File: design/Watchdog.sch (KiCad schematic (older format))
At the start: 23 parts, among them U401 74LV14, U402 74LVC2G00, U403 STWD100xxWY, U404 STWD100xxWY, U405 74AHC157

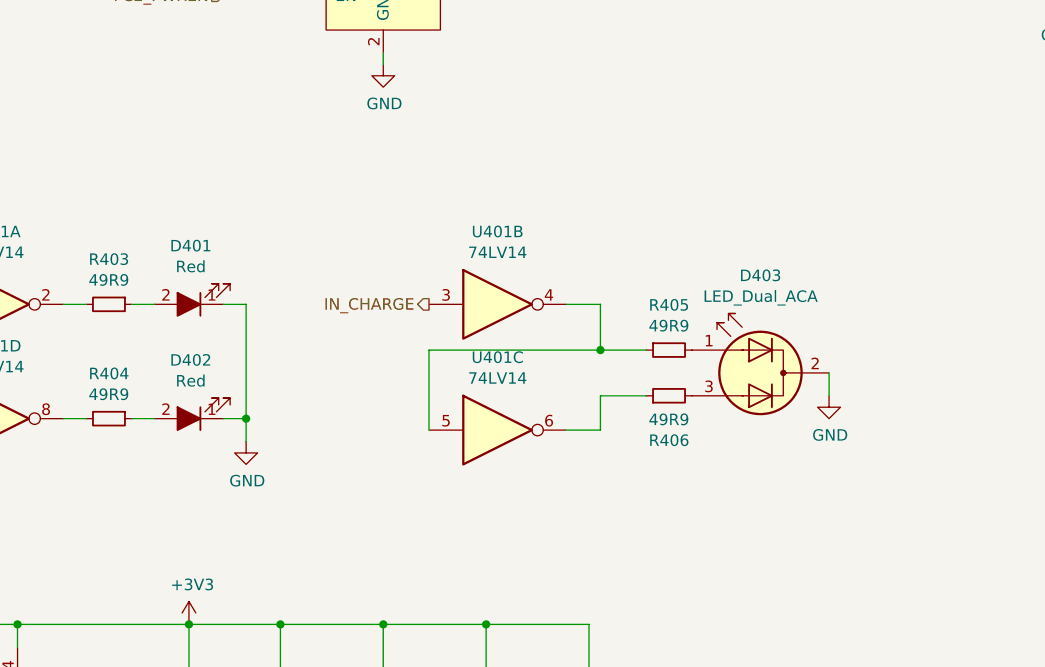
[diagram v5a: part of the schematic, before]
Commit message: Adding smaller light pipe and compressing power input
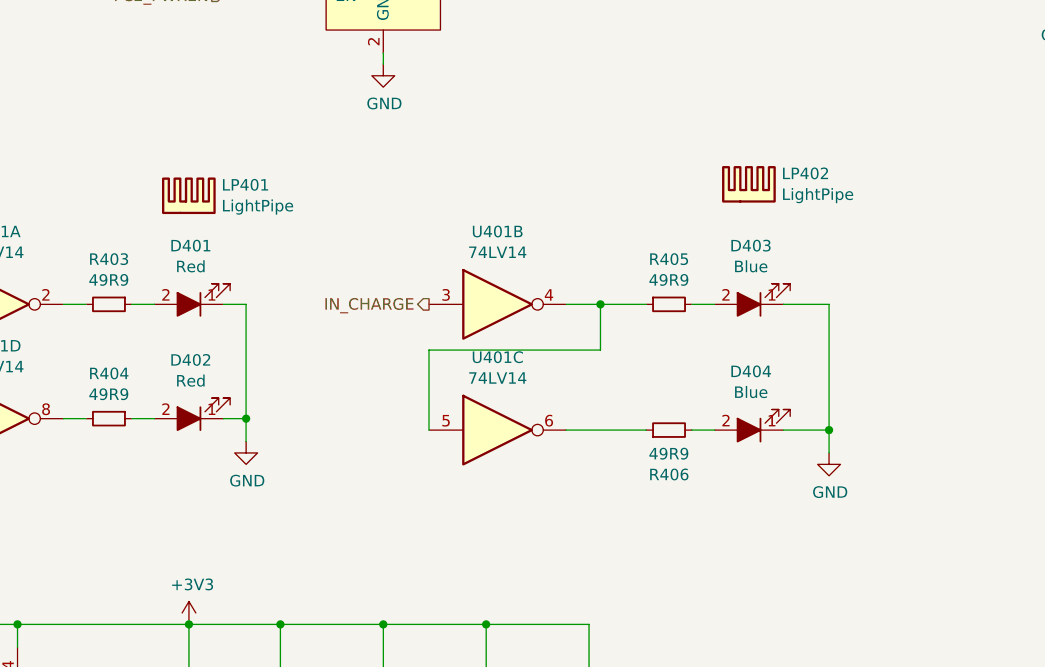
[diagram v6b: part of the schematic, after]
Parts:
- removed D403: LED_Dual_ACA, LEDs:WP130WDT, symbol Device:LED_Dual_ACA
- added D403, D404: Blue, LED_SMD:LED_1206_3216Metric, symbol Device:LED_ALT
- added LP401, LP402: LightPipe, LEDs:Lumex_LPF-C012303S, symbol CommsCard:LightPipe
- D401, D402: footprint LED_THT:LED_D5.0mm_Horizontal_O6.35mm_Z9.0mm -> LED_SMD:LED_1206_3216Metric; mpn LTL-523-11 -> 150120RS75000
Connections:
- net GND: now also D403.1 (K), D404.1 (K)
- net at R405.2: now also D403.2 (A)
- net at R406.2: now also D404.2 (A)
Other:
- moved on the sheet: R405, R406
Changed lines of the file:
@@
 F 0 "D401" H 3592 4445 50  0000 C CNN
 F 1 "Red" H 3592 4536 50  0000 C CNN
-F 2 "LED_THT:LED_D5.0mm_Horizontal_O6.35mm_Z9.0mm" H 3600 4700 50  0001 C CNN
-F 3 "http://optoelectronics.liteon.com/upload/download/DS-20-92-0408/LTL-523-11.pdf" H 3600 4700 50  0001 C CNN
-F 4 "LTL-523-11" H 3600 4700 50  0001 C CNN "mpn"
+F 2 "LED_SMD:LED_1206_3216Metric" H 3600 4700 50  0001 C CNN
+F 3 "http://katalog.we-online.de/led/datasheet/150120RS75000.pdf" H 3600 4700 50  0001 C CNN
+F 4 "150120RS75000" H 3600 4700 50  0001 C CNN "mpn"
 	1    3600 4700
 	-1   0    0    1
@@
 F 0 "D402" H 3592 4945 50  0000 C CNN
 F 1 "Red" H 3592 5036 50  0000 C CNN
-F 2 "LED_THT:LED_D5.0mm_Horizontal_O6.35mm_Z9.0mm" H 3600 5200 50  0001 C CNN
-F 3 "http://optoelectronics.liteon.com/upload/download/DS-20-92-0408/LTL-523-11.pdf" H 3600 5200 50  0001 C CNN
-F 4 "LTL-523-11" H 3600 5200 50  0001 C CNN "mpn"
+F 2 "LED_SMD:LED_1206_3216Metric" H 3600 5200 50  0001 C CNN
+F 3 "http://katalog.we-online.de/led/datasheet/150120RS75000.pdf" H 3600 5200 50  0001 C CNN
+F 4 "150120RS75000" H 3600 5200 50  0001 C CNN "mpn"
 	1    3600 5200
 	-1   0    0    1
@@
 	3    4950 5250
 	1    0    0    -1
-$EndComp
-$Comp
-L Device:LED_Dual_ACA D403
-U 1 1 5A84646B
-P 6100 5000
-F 0 "D403" H 6100 5425 50  0000 C CNN
-F 1 "LED_Dual_ACA" H 6100 5334 50  0000 C CNN
-F 2 "LEDs:WP130WDT" H 6100 5000 50  0001 C CNN
-F 3 "http://www.kingbrightusa.com/images/catalog/SPEC/WP130WDT-EYW.pdf" H 6100 5000 50  0001 C CNN
-F 4 "WP130WDT/EYW" H 6100 5000 50  0001 C CNN "mpn"
-	1    6100 5000
-	-1   0    0    -1
 $EndComp
 $Comp
@@
 L Device:R_Small R405
 U 1 1 5A846591
-P 5700 4900
-F 0 "R405" V 5504 4900 50  0000 C CNN
-F 1 "49R9" V 5595 4900 50  0000 C CNN
-F 2 "Resistor_SMD:R_0603_1608Metric" H 5700 4900 50  0001 C CNN
-F 3 "https://www.seielect.com/Catalog/SEI-rncp.pdf" H 5700 4900 50  0001 C CNN
-F 4 "RNCP0603FTD49R9" H 5700 4900 50  0001 C CNN "mpn"
-	1    5700 4900
+P 5700 4700
+F 0 "R405" V 5504 4700 50  0000 C CNN
+F 1 "49R9" V 5595 4700 50  0000 C CNN
+F 2 "Resistor_SMD:R_0603_1608Metric" H 5700 4700 50  0001 C CNN
+F 3 "https://www.seielect.com/Catalog/SEI-rncp.pdf" H 5700 4700 50  0001 C CNN
+F 4 "RNCP0603FTD49R9" H 5700 4700 50  0001 C CNN "mpn"
+	1    5700 4700
 	0    -1   1    0
 $EndComp
@@
 	5400 4700 5250 4700
 Wire Wire Line
-	5400 4900 5600 4900
-Connection ~ 5400 4900
+	5400 4700 5600 4700
 Wire Wire Line
 	5400 4900 5400 4700
@@
 L Device:R_Small R406
 U 1 1 5A84C00E
-P 5700 5100
-F 0 "R406" V 5504 5100 50  0000 C CNN
-F 1 "49R9" V 5595 5100 50  0000 C CNN
-F 2 "Resistor_SMD:R_0603_1608Metric" H 5700 5100 50  0001 C CNN
-F 3 "https://www.seielect.com/Catalog/SEI-rncp.pdf" H 5700 5100 50  0001 C CNN
-F 4 "RNCP0603FTD49R9" H 5700 5100 50  0001 C CNN "mpn"
-	1    5700 5100
+P 5700 5250
+F 0 "R406" V 5504 5250 50  0000 C CNN
+F 1 "49R9" V 5595 5250 50  0000 C CNN
+F 2 "Resistor_SMD:R_0603_1608Metric" H 5700 5250 50  0001 C CNN
+F 3 "https://www.seielect.com/Catalog/SEI-rncp.pdf" H 5700 5250 50  0001 C CNN
+F 4 "RNCP0603FTD49R9" H 5700 5250 50  0001 C CNN "mpn"
+	1    5700 5250
 	0    -1   -1   0
 $EndComp
-Wire Wire Line
-	5600 5100 5400 5100
-Wire Wire Line
-	5400 5100 5400 5250
-Wire Wire Line
-	5400 5250 5250 5250
 Text HLabel 4650 4700 0    50   Output ~ 0
 IN_CHARGE
@@
 L power:GND #PWR0410
 U 1 1 5A8484FB
-P 6400 5100
-F 0 "#PWR0410" H 6400 4850 50  0001 C CNN
-F 1 "GND" H 6405 4927 50  0000 C CNN
-F 2 "" H 6400 5100 50  0001 C CNN
-F 3 "" H 6400 5100 50  0001 C CNN
-	1    6400 5100
-	1    0    0    -1
-$EndComp
-Wire Wire Line
-	6400 5100 6400 5000
+P 6400 5350
+F 0 "#PWR0410" H 6400 5100 50  0001 C CNN
+F 1 "GND" H 6405 5177 50  0000 C CNN
+F 2 "" H 6400 5350 50  0001 C CNN
+F 3 "" H 6400 5350 50  0001 C CNN
+	1    6400 5350
+	1    0    0    -1
+$EndComp
 Wire Wire Line
 	2450 6550 2450 6100
@@
 Wire Wire Line
 	6350 1950 6450 1950
+$Comp
+L Device:LED_ALT D403
+U 1 1 5AB14DB8
+P 6050 4700
+F 0 "D403" H 6042 4445 50  0000 C CNN
+F 1 "Blue" H 6042 4536 50  0000 C CNN
+F 2 "LED_SMD:LED_1206_3216Metric" H 6050 4700 50  0001 C CNN
+F 3 "http://katalog.we-online.de/led/datasheet/150120BS75000.pdf" H 6050 4700 50  0001 C CNN
+F 4 "150120BS75000" H 6050 4700 50  0001 C CNN "mpn"
+	1    6050 4700
+	-1   0    0    1
+$EndComp
+$Comp
+L Device:LED_ALT D404
+U 1 1 5AB14E28
+P 6050 5250
+F 0 "D404" H 6042 4995 50  0000 C CNN
+F 1 "Blue" H 6042 5086 50  0000 C CNN
+F 2 "LED_SMD:LED_1206_3216Metric" H 6050 5250 50  0001 C CNN
+F 3 "http://katalog.we-online.de/led/datasheet/150120BS75000.pdf" H 6050 5250 50  0001 C CNN
+F 4 "150120BS75000" H 6050 5250 50  0001 C CNN "mpn"
+	1    6050 5250
+	-1   0    0    1
+$EndComp
+Connection ~ 5400 4700
+Wire Wire Line
+	5250 5250 5600 5250
+Wire Wire Line
+	6400 4700 6200 4700
+Wire Wire Line
+	6400 4700 6400 5250
+Wire Wire Line
+	6200 5250 6400 5250
+Connection ~ 6400 5250
+Wire Wire Line
+	6400 5250 6400 5350
+Wire Wire Line
+	5800 5250 5900 5250
+Wire Wire Line
+	5800 4700 5900 4700
+$Comp
+L CommsCard:LightPipe LP402
+U 1 1 5AB20252
+P 6050 4250
+F 0 "LP402" H 6192 4371 50  0000 L CNN
+F 1 "LightPipe" H 6192 4280 50  0000 L CNN
+F 2 "LEDs:Lumex_LPF-C012303S" H 6062 4250 50  0001 C CNN
+F 3 "" H 6062 4250 50  0001 C CNN
+	1    6050 4250
+	1    0    0    -1
+$EndComp
+$Comp
+L CommsCard:LightPipe LP401
+U 1 1 5AB202B8
+P 3600 4300
+F 0 "LP401" H 3742 4421 50  0000 L CNN
+F 1 "LightPipe" H 3742 4330 50  0000 L CNN
+F 2 "LEDs:Lumex_LPF-C012303S" H 3612 4300 50  0001 C CNN
+F 3 "" H 3612 4300 50  0001 C CNN
+	1    3600 4300
+	1    0    0    -1
+$EndComp
 $EndSCHEMATC
